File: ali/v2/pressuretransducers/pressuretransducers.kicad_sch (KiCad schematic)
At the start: 4 parts

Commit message: Minor updates
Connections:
- no-connect marks 0 -> 1
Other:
- sheet Analog 1 ports: added CLK; removed none
- sheet Analog 2 ports: added CLK; removed none
- sheet Microcontroller ports: added ADC_CLK, ADC_DRDY, ADC_MISO, ADC_MOSI, ADC_RESET, ADC_SCLK; removed ADC1_DRDY, ADC1_~{RST}, ADC2_DRDY, ADC2_~{RST}, SPI1_MISO, SPI1_MOSI, SPI1_SCK

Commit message: The other half of the great 10.0.6 migration
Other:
- sheet Analog 2 renamed Analog 2 (pa`ge 5)
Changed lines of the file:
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@@
 			(color 0 0 0 0)
 		)
-		(property "Sheetname" "Analog 2"
+		(property "Sheetname" "Analog 2 (pa`ge 5)"
 			(at 198.12 155.4984 0)
 			(show_name no)

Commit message: Commentary
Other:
- sheet Analog 2 (pa`ge 5) renamed Analog 2
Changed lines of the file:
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@@
 			(color 0 0 0 0)
 		)
-		(property "Sheetname" "Analog 2 (pa`ge 5)"
+		(property "Sheetname" "Analog 2"
 			(at 198.12 155.4984 0)
 			(show_name no)
@@
 			)
 		)
-		(pin "ADC_RESET" output
+		(pin "ADC_RESET" input
 			(at 171.45 149.86 0)
 			(effects

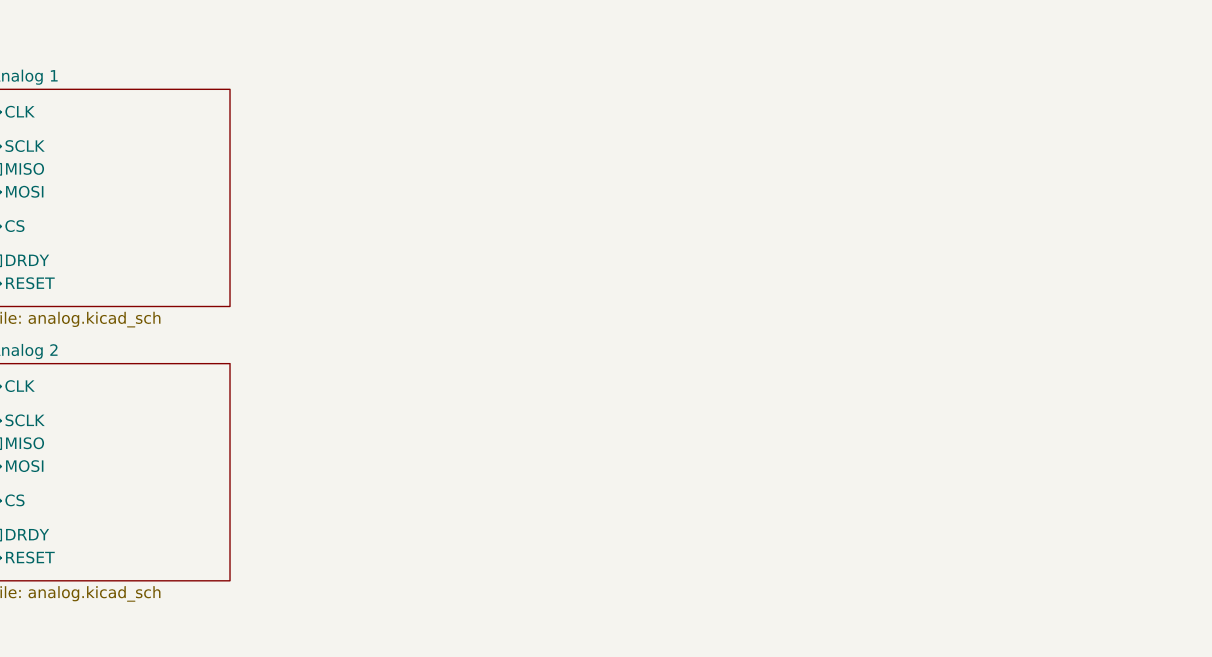
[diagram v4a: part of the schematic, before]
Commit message: Document setup, update template, and use an ampersand when referring to APRL
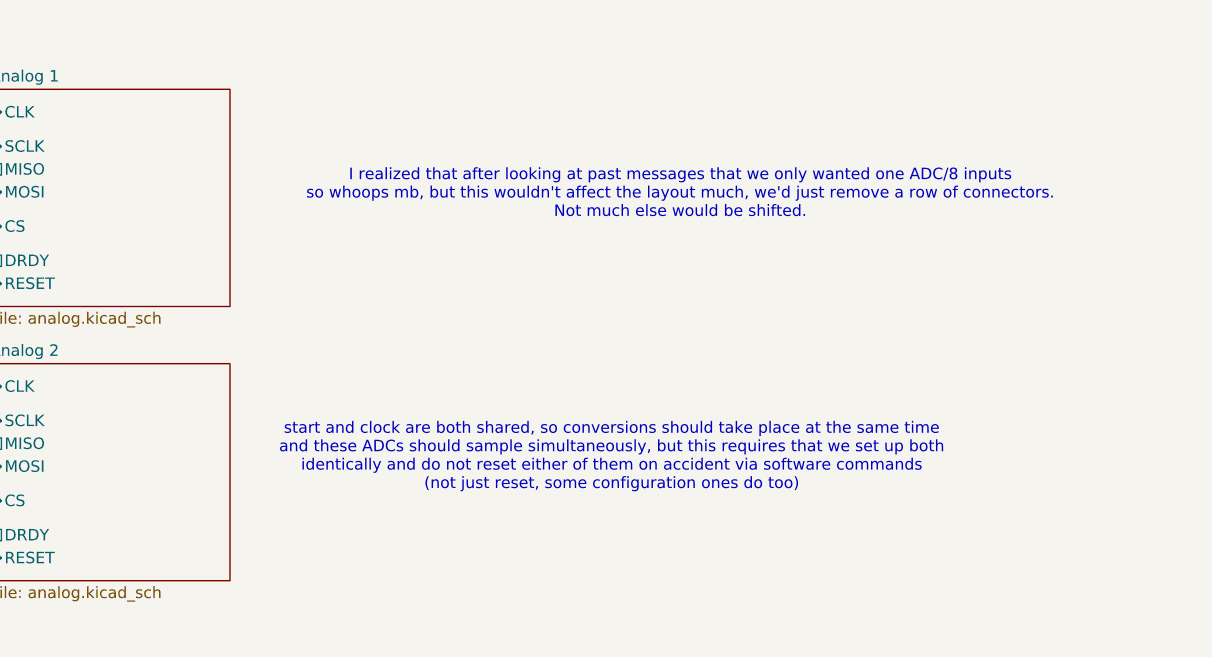
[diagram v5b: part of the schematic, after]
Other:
- note added: "I realized that after looking at past messages that we only wanted one ADC/8 inputs so whoops mb, but this wouldn't affect the layout much, we'd just remove a row of connectors. Not much else would be shifted."
- note added: "start and clock are both shared, so conversions should take place at the same time and these ADCs should sample simultaneously, but this requires that we set up both identically and do not reset either of them on accident via software commands (not just reset, some configuration ones do too)"

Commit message: Begin prep for second board review
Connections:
- no-connect marks 1 -> 0
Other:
- sheet Analog 1 ports: added none; removed CLK
- sheet Analog 2 ports: added none; removed CLK
- sheet Microcontroller ports: added ADC_DRDY1, ADC_DRDY2; removed ADC_CLK, ADC_DRDY
- note removed: "I realized that after looking at past messages that we only wanted one ADC/8 inputs so whoops mb, but this wouldn't affect the layout much, we'd just remove a row of connectors. Not much else would be shifted."
- note removed: "start and clock are both shared, so conversions should take place at the same time and these ADCs should sample simultaneously, but this requires that we set up both identically and do not reset either of them on accident via software commands (not just reset, some configuration ones do too)"
